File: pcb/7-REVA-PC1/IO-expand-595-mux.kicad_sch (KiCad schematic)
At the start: 47 parts, among them Q2 2N7002KT, U10 LM358_DFN, U11 LM358_DFN, U12 LM358_DFN, U13 LM358_DFN, U17 WS72324Q, U18 WS72324Q, U2 74LVC8T245BQ, U4 XL9555QF24, U402 CD4067, U5 WS72324Q, U503 74HCT245BQ, U9 LM358_DFN

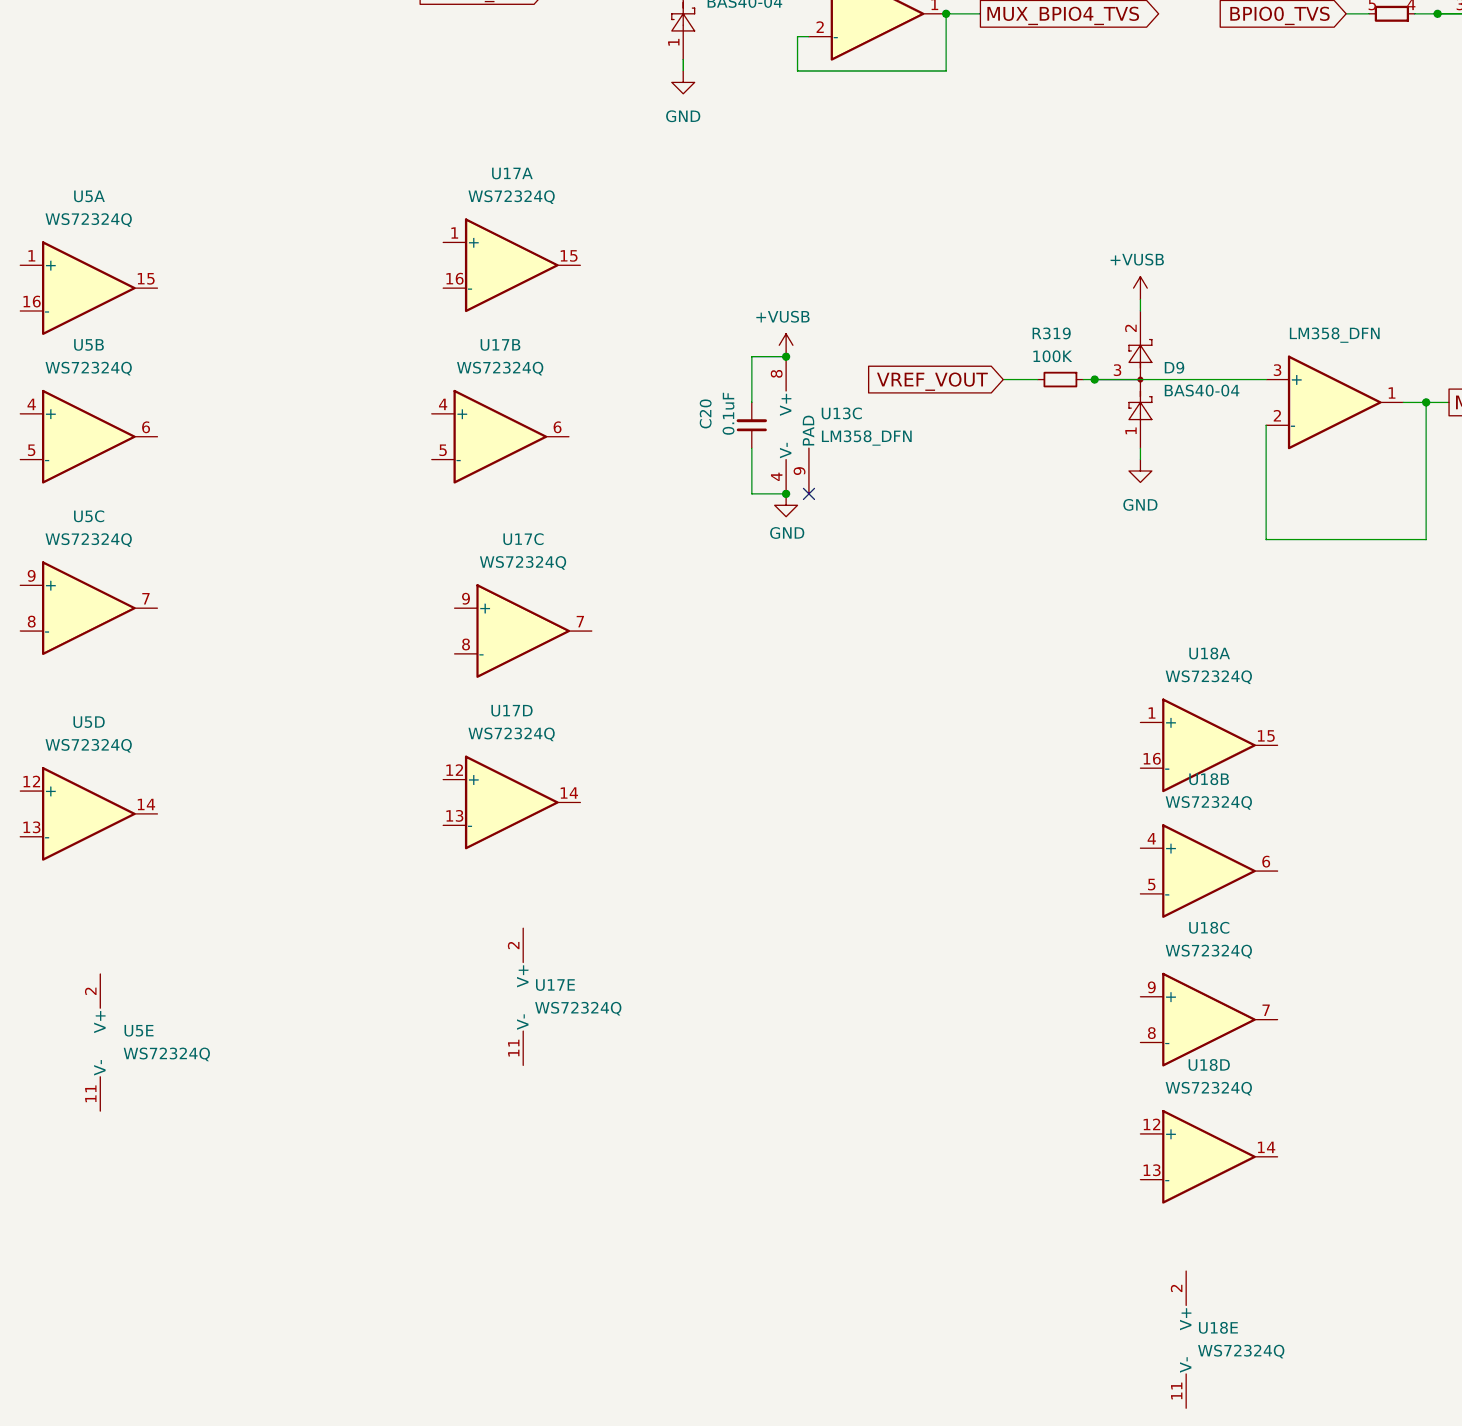
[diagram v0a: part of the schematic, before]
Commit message: Remove DNF footprints, locate PWM pins for power supply adjustment. Change PWM op-amp to DFN and buffer also the CURRENT_ADJ. Remove a FET gate resistor from current limiter.
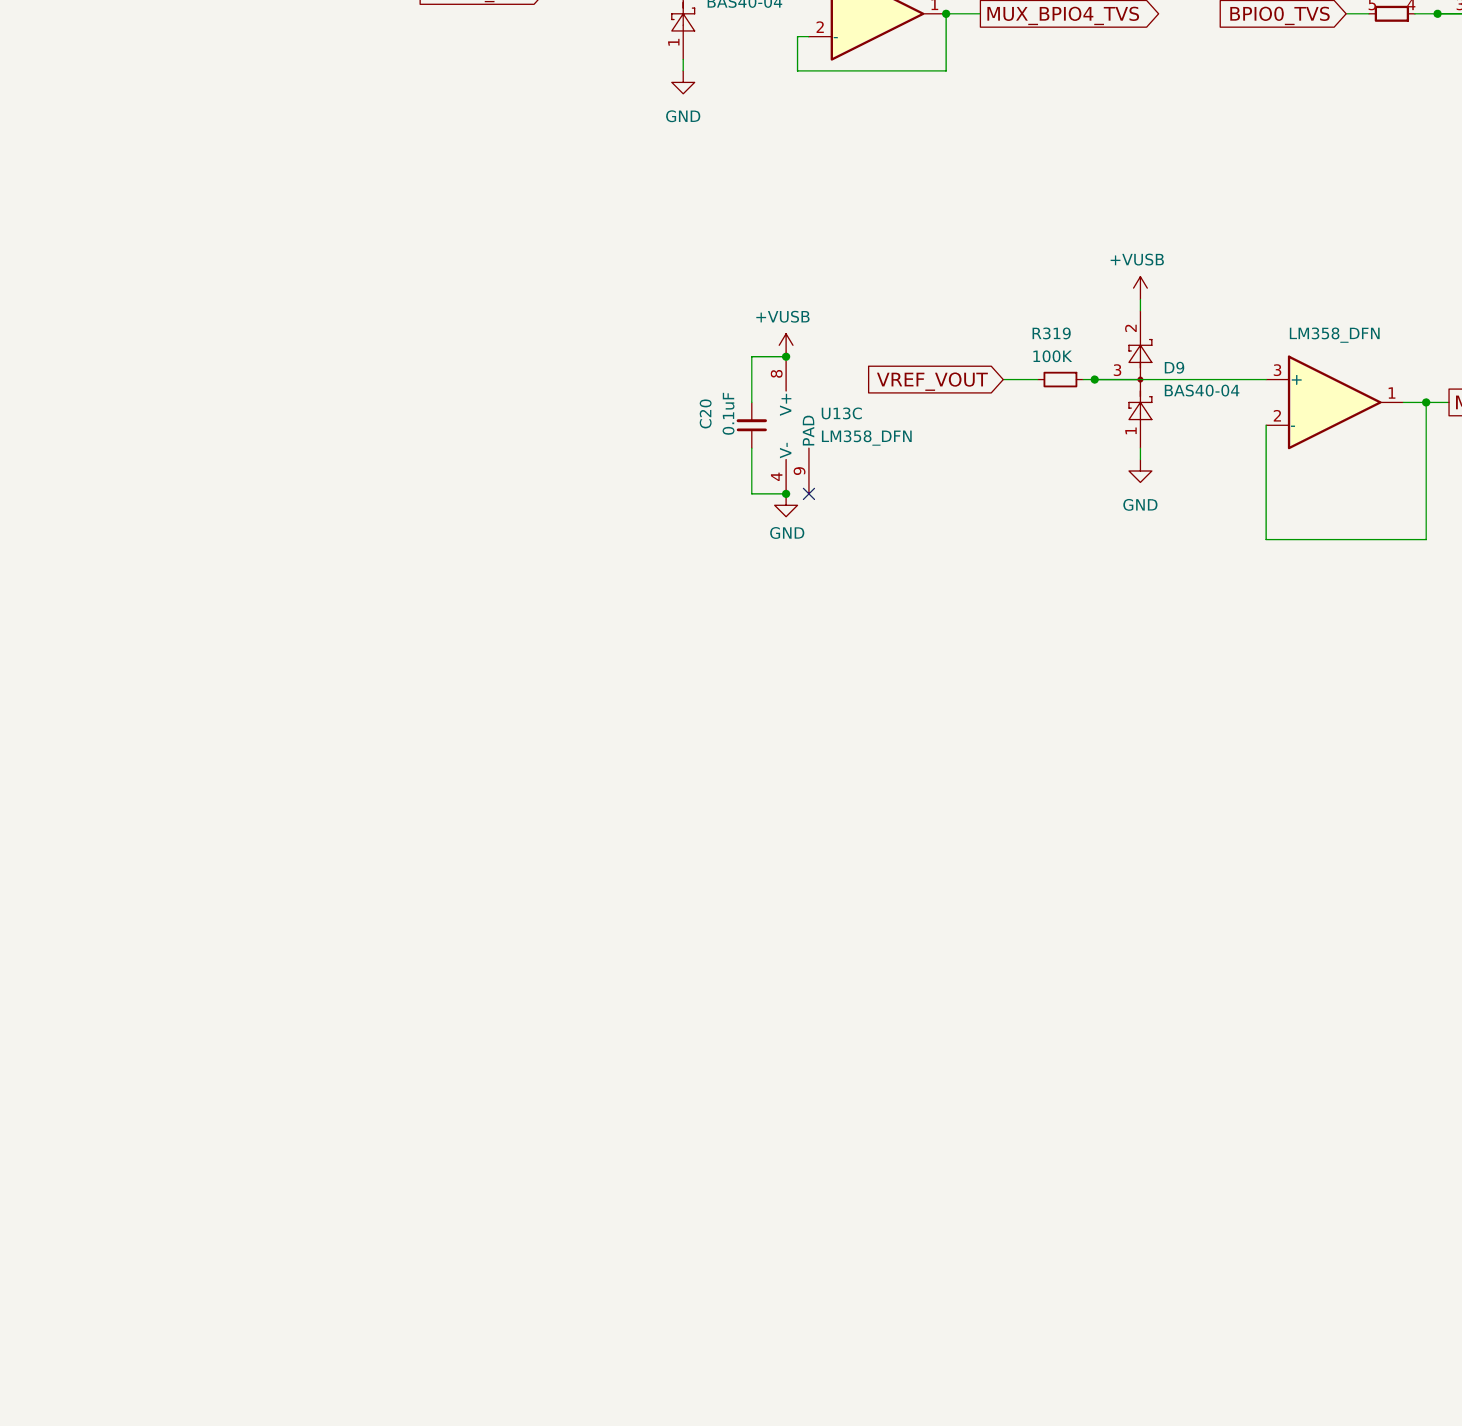
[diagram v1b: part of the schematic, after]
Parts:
- removed U17, U18, U5: WS72324Q, Package_DFN_QFN:QFN-16-1EP_3x3mm_P0.5mm_EP1.7x1.7mm, symbol ws72324q:WS72324Q

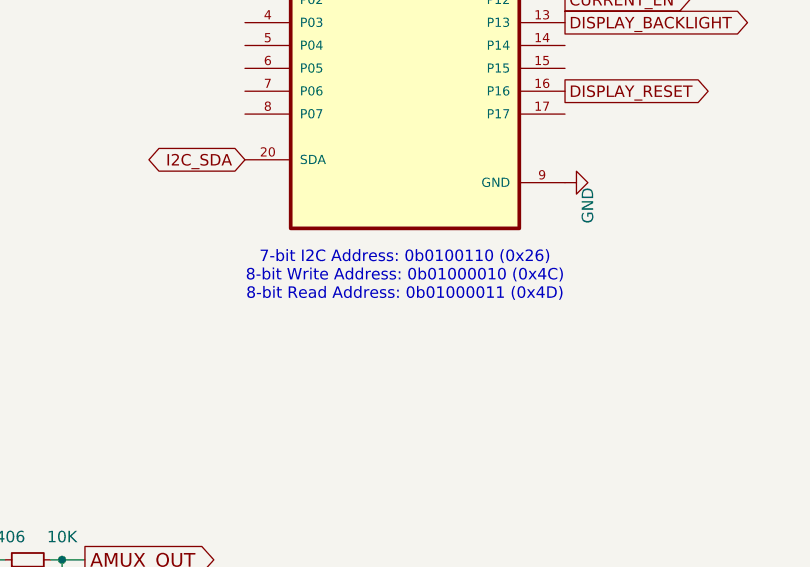
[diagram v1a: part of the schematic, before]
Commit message: Remove VREG bypass diode. Fix XL9555 I2C address
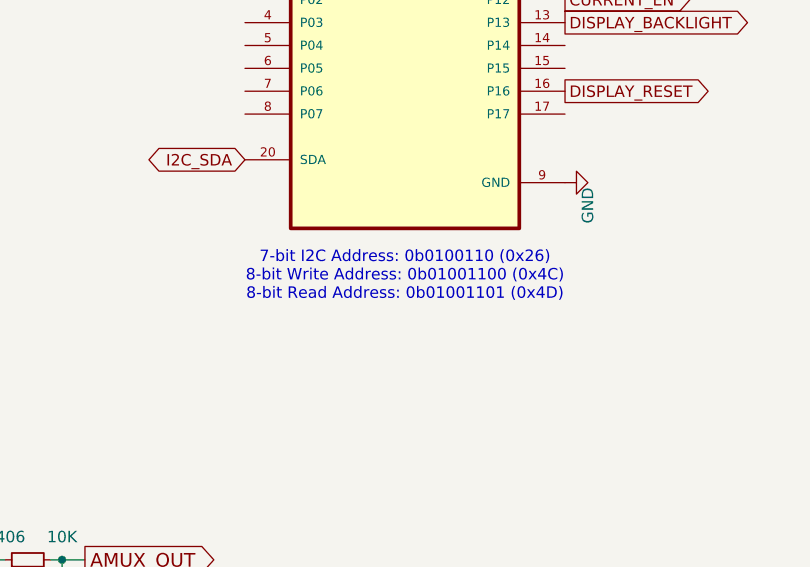
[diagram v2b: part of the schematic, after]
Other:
- note added: "7-bit I2C Address: 0b0100110 (0x26) 8-bit Write Address: 0b01001100 (0x4C) 8-bit Read Address: 0b01001101 (0x4D)"
- note removed: "7-bit I2C Address: 0b0100110 (0x26) 8-bit Write Address: 0b01000010 (0x4C) 8-bit Read Address: 0b01000011 (0x4D)"
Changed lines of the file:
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@@
 		)
 	)
-	(text "7-bit I2C Address: 0b0100110 (0x26)\n8-bit Write Address: 0b01000010 (0x4C)\n8-bit Read Address: 0b01000011 (0x4D)"
+	(text "7-bit I2C Address: 0b0100110 (0x26)\n8-bit Write Address: 0b01001100 (0x4C)\n8-bit Read Address: 0b01001101 (0x4D)"
 		(exclude_from_sim no)
 		(at 354.33 181.864 0)

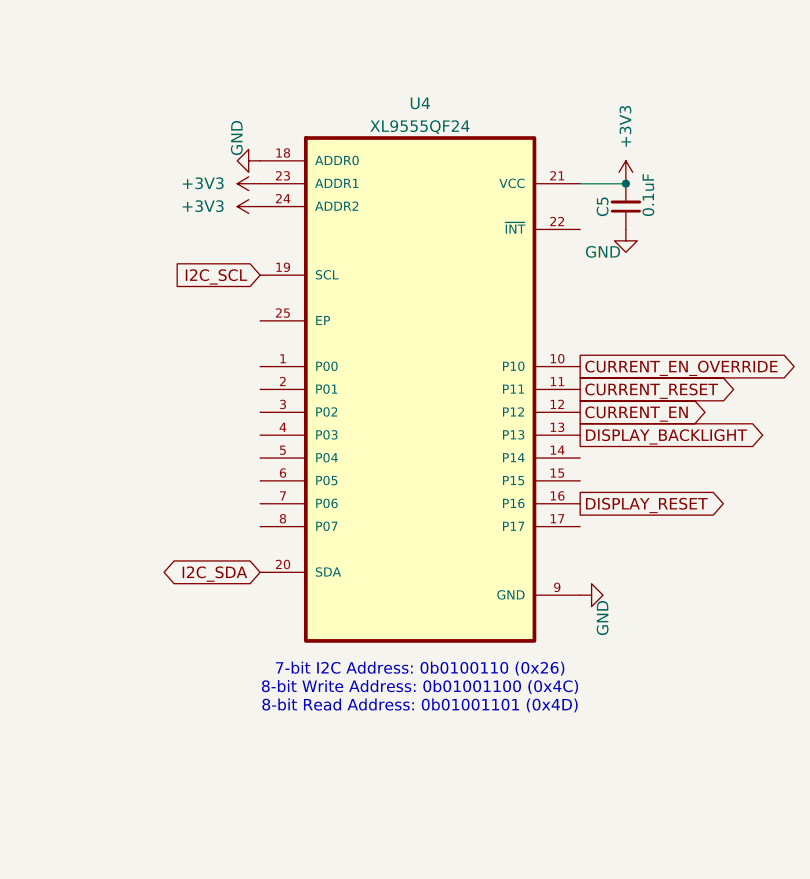
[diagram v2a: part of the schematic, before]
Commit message: Change XL9555 I2C address to advance from TCA6416ARTWR. Change adjustable voltage regulator to correct part number.
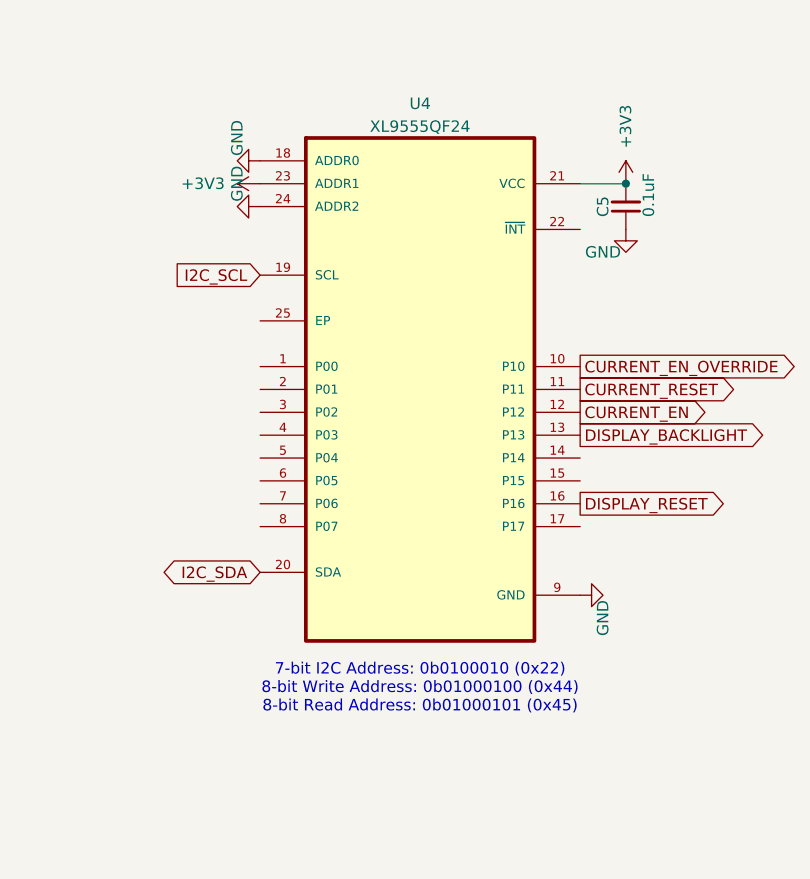
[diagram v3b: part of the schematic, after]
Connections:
- net +3V3: no longer U4.24 (ADDR2)
- net GND: now also U4.24 (ADDR2)
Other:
- note added: "7-bit I2C Address: 0b0100010 (0x22) 8-bit Write Address: 0b01000100 (0x44) 8-bit Read Address: 0b01000101 (0x45)"
- note removed: "7-bit I2C Address: 0b0100110 (0x26) 8-bit Write Address: 0b01001100 (0x4C) 8-bit Read Address: 0b01001101 (0x4D)"
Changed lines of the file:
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@@
 		)
 	)
-	(text "7-bit I2C Address: 0b0100110 (0x26)\n8-bit Write Address: 0b01001100 (0x4C)\n8-bit Read Address: 0b01001101 (0x4D)"
+	(text "7-bit I2C Address: 0b0100010 (0x22)\n8-bit Write Address: 0b01000100 (0x44)\n8-bit Read Address: 0b01000101 (0x45)"
 		(exclude_from_sim no)
 		(at 354.33 181.864 0)
@@
 	)
 	(symbol
+		(lib_id "power:GND")
+		(at 336.55 128.27 270)
+		(unit 1)
+		(exclude_from_sim no)
+		(in_bom yes)
+		(on_board yes)
+		(dnp no)
+		(property "Reference" "#PWR048"
+			(at 330.2 128.27 0)
+			(effects
+				(font
+					(size 1.27 1.27)
+				)
+				(hide yes)
+			)
+		)
+		(property "Value" "GND"
+			(at 334.01 125.73 0)
+			(effects
+				(font
+					(size 1.27 1.27)
+				)
+			)
+		)
+		(property "Footprint" ""
+			(at 336.55 128.27 0)
+			(effects
+				(font
+					(size 1.27 1.27)
+				)
+				(hide yes)
+			)
+		)
+		(property "Datasheet" ""
+			(at 336.55 128.27 0)
+			(effects
+				(font
+					(size 1.27 1.27)
+				)
+				(hide yes)
+			)
+		)
+		(property "Description" ""
+			(at 336.55 128.27 0)
+			(effects
+				(font
+					(size 1.27 1.27)
+				)
+				(hide yes)
+			)
+		)
+		(pin "1"
+		)
+		(instances
+			(project "7-REVA-PC1"
+				(path "/1f56410a-eaac-4444-b0f7-cfd3531e22ac/00000000-0000-0000-0000-000060e58ecc"
+					(reference "#PWR048")
+					(unit 1)
+				)
+			)
+		)
+	)
+	(symbol
 		(lib_id "dp-rarray:R_Array")
 		(at 125.73 175.26 270)
@@
 					(unit 1)
 				)
-			)
-		)
-	)
-	(symbol
-		(lib_id "power:+3V3")
-		(at 336.55 128.27 90)
-		(unit 1)
-		(exclude_from_sim no)
-		(in_bom yes)
-		(on_board yes)
-		(dnp no)
-		(property "Reference" "#PWR048"
-			(at 340.36 128.27 0)
-			(effects
-				(font
-					(size 1.27 1.27)
-				)
-				(hide yes)
-			)
-		)
-		(property "Value" "+3V3"
-			(at 330.2 128.27 90)
-			(effects
-				(font
-					(size 1.27 1.27)
-				)
-			)
-		)
-		(property "Footprint" ""
-			(at 336.55 128.27 0)
-			(effects
-				(font
-					(size 1.27 1.27)
-				)
-				(hide yes)
-			)
-		)
-		(property "Datasheet" ""
-			(at 336.55 128.27 0)
-			(effects
-				(font
-					(size 1.27 1.27)
-				)
-				(hide yes)
-			)
-		)
-		(property "Description" ""
-			(at 336.55 128.27 0)
-			(effects
-				(font
-					(size 1.27 1.27)
-				)
-				(hide yes)
-			)
-		)
-		(pin "1"
-		)
-		(instances
-			(project "7-REV1"
-				(path "/1f56410a-eaac-4444-b0f7-cfd3531e22ac/00000000-0000-0000-0000-000060e58ecc"
-					(reference "#PWR048")
-					(unit 1)
-				)

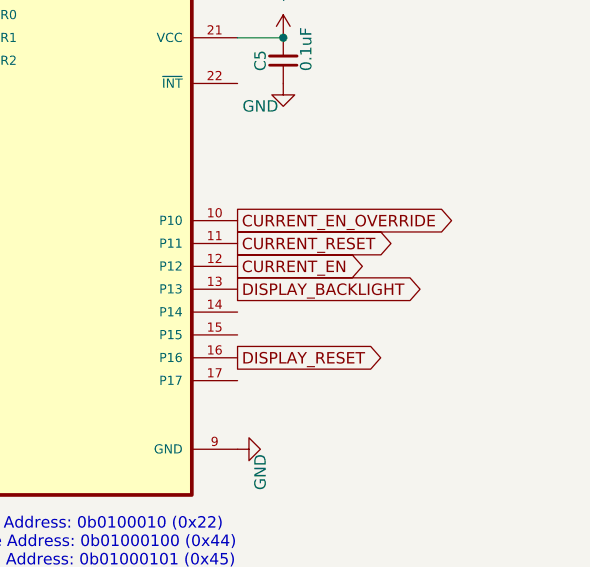
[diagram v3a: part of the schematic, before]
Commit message: Show that XL9555 is not connected.
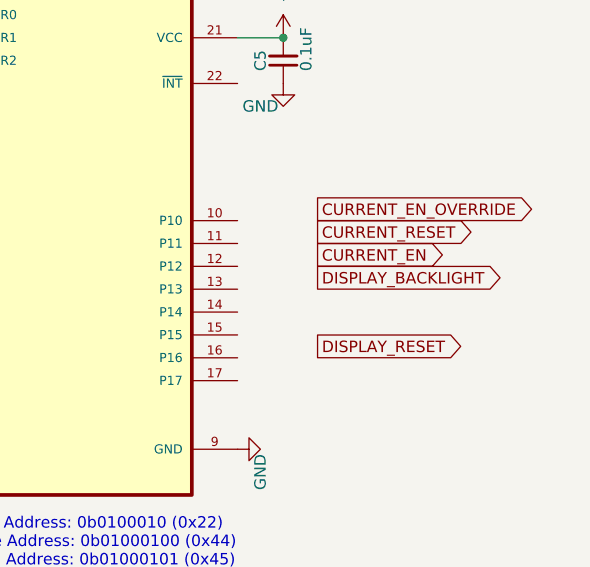
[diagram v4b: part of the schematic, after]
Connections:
- net CURRENT_EN: no longer U4.12 (P12)
- net CURRENT_EN_OVERRIDE: no longer U4.10 (P10)
- net CURRENT_RESET: no longer U4.11 (P11)
- net DISPLAY_BACKLIGHT: no longer U4.13 (P13)
- net DISPLAY_RESET: no longer U4.16 (P16)
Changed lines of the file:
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@@
 	(global_label "CURRENT_RESET"
 		(shape output)
-		(at 372.11 148.59 0)
-		(effects
-			(font
-				(size 1.27 1.27)
-			)
-			(justify left)
-		)
-		(property "Intersheetrefs" "${INTERSHEET_REFS}"
-			(at 372.11 148.59 0)
+		(at 381 147.32 0)
+		(effects
+			(font
+				(size 1.27 1.27)
+			)
+			(justify left)
+		)
+		(property "Intersheetrefs" "${INTERSHEET_REFS}"
+			(at 381 147.32 0)
 			(effects
 				(font
@@
 	(global_label "DISPLAY_RESET"
 		(shape output)
-		(at 372.11 161.29 0)
-		(effects
-			(font
-				(size 1.27 1.27)
-			)
-			(justify left)
-		)
-		(property "Intersheetrefs" "${INTERSHEET_REFS}"
-			(at 372.11 161.29 0)
+		(at 381 160.02 0)
+		(effects
+			(font
+				(size 1.27 1.27)
+			)
+			(justify left)
+		)
+		(property "Intersheetrefs" "${INTERSHEET_REFS}"
+			(at 381 160.02 0)
 			(effects
 				(font
@@
 	(global_label "CURRENT_EN_OVERRIDE"
 		(shape output)
-		(at 372.11 146.05 0)
-		(effects
-			(font
-				(size 1.27 1.27)
-			)
-			(justify left)
-		)
-		(property "Intersheetrefs" "${INTERSHEET_REFS}"
-			(at 372.11 146.05 0)
+		(at 381 144.78 0)
+		(effects
+			(font
+				(size 1.27 1.27)
+			)
+			(justify left)
+		)
+		(property "Intersheetrefs" "${INTERSHEET_REFS}"
+			(at 381 144.78 0)
 			(effects
 				(font
@@
 	(global_label "DISPLAY_BACKLIGHT"
 		(shape output)
-		(at 372.11 153.67 0)
-		(effects
-			(font
-				(size 1.27 1.27)
-			)
-			(justify left)
-		)
-		(property "Intersheetrefs" "${INTERSHEET_REFS}"
-			(at 372.11 153.67 0)
+		(at 381 152.4 0)
+		(effects
+			(font
+				(size 1.27 1.27)
+			)
+			(justify left)
+		)
+		(property "Intersheetrefs" "${INTERSHEET_REFS}"
+			(at 381 152.4 0)
 			(effects
 				(font
@@
 	(global_label "CURRENT_EN"
 		(shape output)
-		(at 372.11 151.13 0)
-		(effects
-			(font
-				(size 1.27 1.27)
-			)
-			(justify left)
-		)
-		(property "Intersheetrefs" "${INTERSHEET_REFS}"
-			(at 372.11 151.13 0)
-			(effects
-				(font
+		(at 381 149.86 0)
+		(effects
+			(font
+				(size 1.27 1.27)
+			)
+			(justify left)
+		)
+		(property "Intersheetrefs" "${INTERSHEET_REFS}"
+			(at 381 149.86 0)
+			(effects
+				(font

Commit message: 7R1 PCB routed
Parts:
- added RN10, RN11: 1M, Resistor_SMD:R_Array_Convex_4x0402, symbol dp-rarray:R_Array
- D1, D2, D3, D4, D5, D6, D7, D8, D9, Q2: footprint Package_TO_SOT_SMD:SOT-523 -> library:SOT-523
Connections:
- net BPIO0_TVS: now also RN10.1 (R1.1)
- net BPIO1_TVS: now also RN10.2 (R1.1)
- net BPIO2_TVS: now also RN10.3 (R1.1)
- net BPIO3_TVS: now also RN10.4 (R1.1)
- net BPIO4_TVS: now also RN11.1 (R1.1)
- net BPIO5_TVS: now also RN11.2 (R1.1)
- net BPIO6_TVS: now also RN11.3 (R1.1)
- net BPIO7_TVS: now also RN11.4 (R1.1)
- net CURRENT_DETECT: now also U4.14 (P14); no longer U402.20 (I11)
- net CURRENT_EN: now also U4.15 (P15)
- net CURRENT_EN_OVERRIDE: now also U4.17 (P17)
- net CURRENT_RESET: now also U4.13 (P13)
- net DISPLAY_BACKLIGHT: now also U4.10 (P10)
- net DISPLAY_RESET: now also U4.11 (P11)
- net GND: now also U4.25 (EP), U402.20 (I11)
- net at U4.1 (P00): now also RN10.8 (R1.8)
- net at U4.2 (P01): now also RN10.7 (R1.8)
- net XL9555_~{INT}: now reaches U4.22 (~{INT})
- net at U4.3 (P02): now also RN10.6 (R1.8)
- net at U4.4 (P03): now also RN10.5 (R1.8)
- net at U4.5 (P04): now also RN11.8 (R1.8)
- net at U4.6 (P05): now also RN11.7 (R1.8)
- net at U4.7 (P06): now also RN11.6 (R1.8)
- net at U4.8 (P07): now also RN11.5 (R1.8)
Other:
- moved on the sheet: C5
